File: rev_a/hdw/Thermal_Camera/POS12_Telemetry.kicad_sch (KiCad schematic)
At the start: 7 parts, among them U501 INA219BxDCN, U502 MCP9804

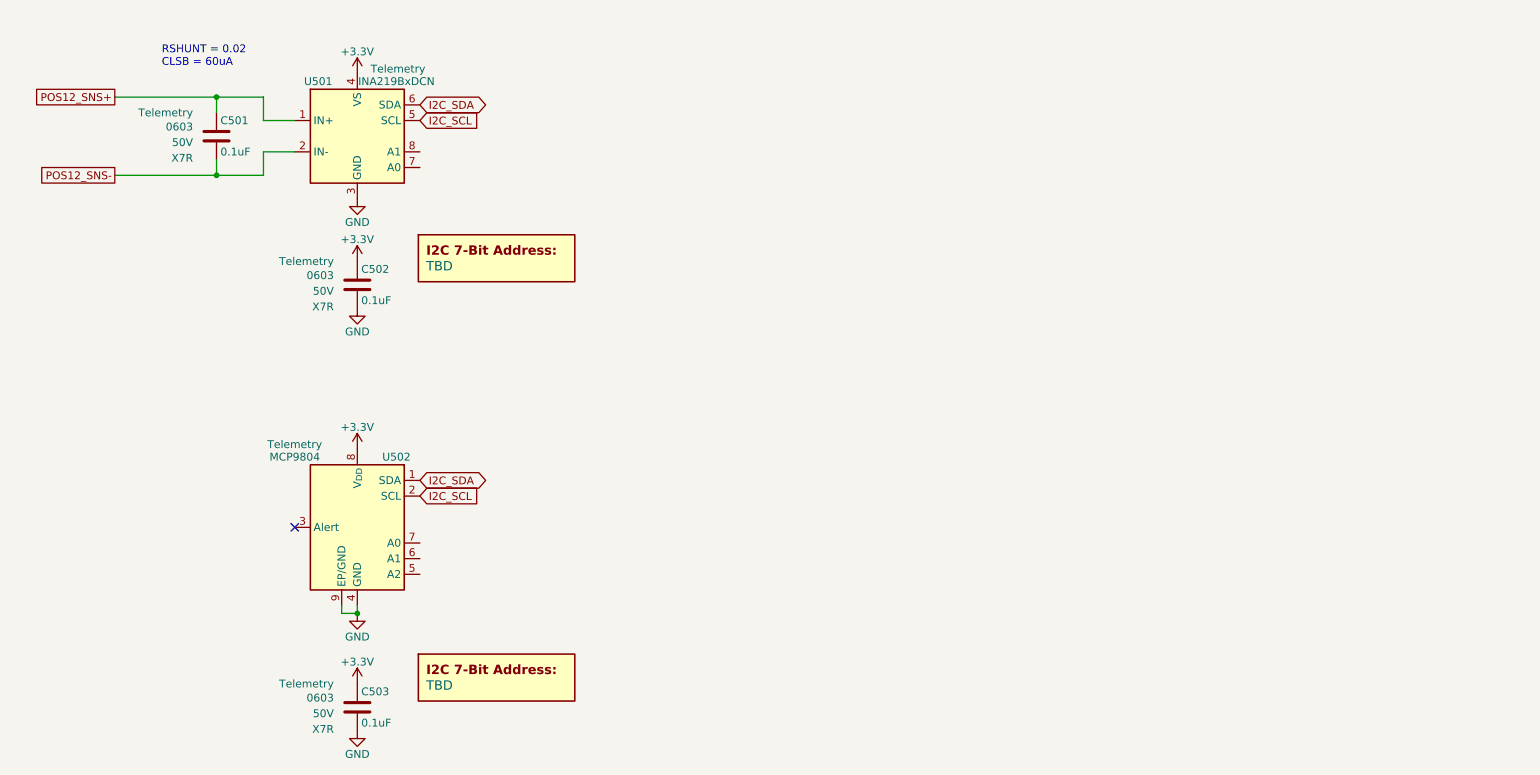
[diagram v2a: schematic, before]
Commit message: changed a lot of circuits from +3.3V to +3.0V VDD
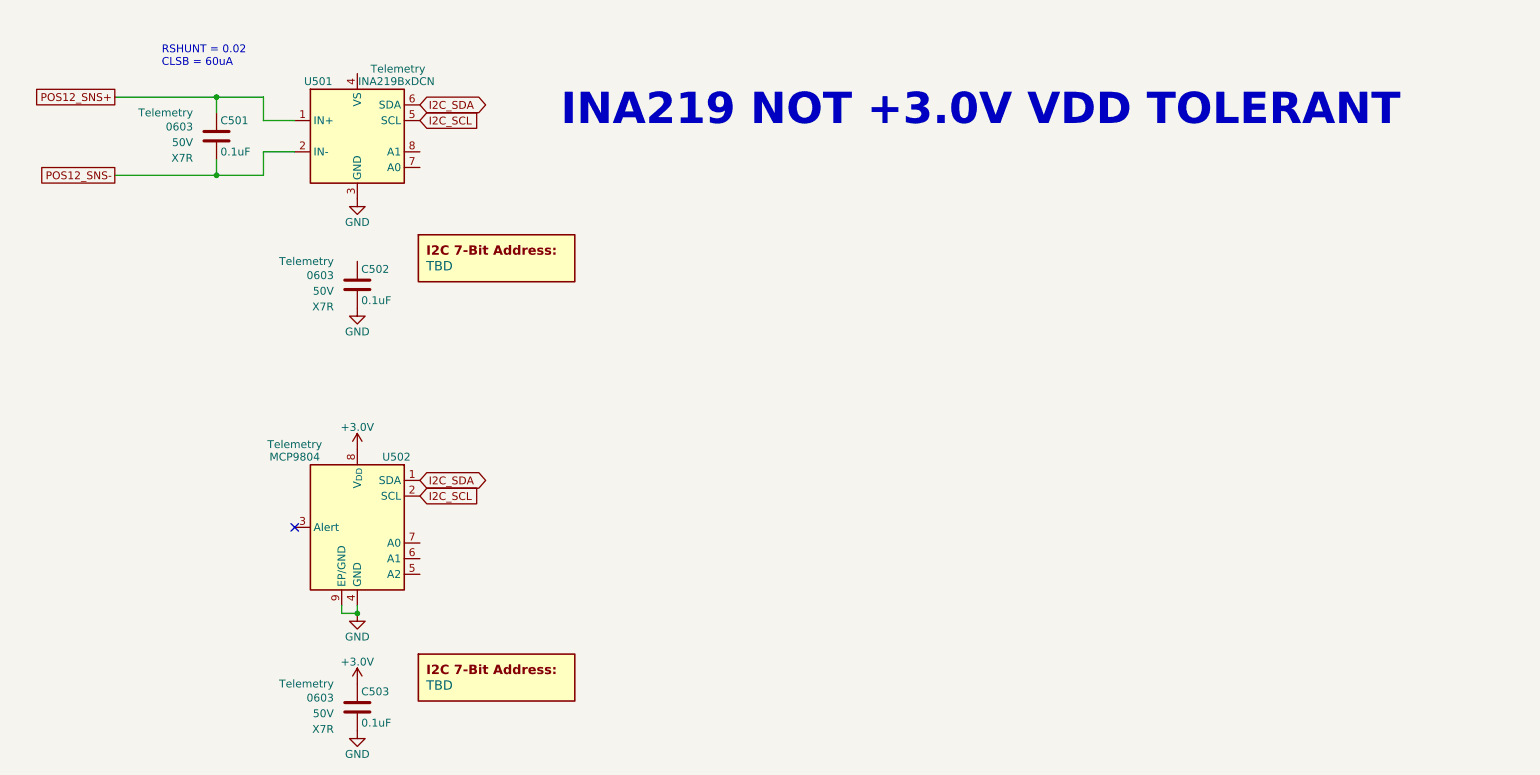
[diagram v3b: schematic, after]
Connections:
- net +3.3V renamed +3.0V
- net +3.0V: no longer C502.1, U501.4 (VS)
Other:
- note added: "INA219 NOT +3.0V VDD TOLERANT"
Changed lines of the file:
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@@
     (effects (font (size 1.27 1.27)) (justify left bottom))
+  )
+  (text "INA219 NOT +3.0V VDD TOLERANT" (at 168.91 50.8 0)
+    (effects (font (face "Courier New") (size 5.08 5.08) (thickness 0.508) bold (color 194 0 0 1)) (justify left bottom))
   )
   (global_label "I2C_SCL" (shape input) (at 146.05 49.53 0) (fields_autoplaced)
@@
     )
   )
+  (symbol (lib_id "Custom Library:+3.0V") (at 135.89 102.87 0) (unit 1)
+    (in_bom yes) (on_board yes) (dnp no)
+    (property "Reference" "#PWR0307" (at 135.89 106.68 0)
+      (effects (font (size 1.27 1.27)) hide)
+    )
+    (property "Value" "+3.0V" (at 135.89 99.314 0)
+      (effects (font (size 1.27 1.27)))
+    )
+    (property "Footprint" "" (at 135.89 102.87 0)
+      (effects (font (size 1.27 1.27)) hide)
+    )
+    (property "Datasheet" "" (at 135.89 102.87 0)
+      (effects (font (size 1.27 1.27)) hide)
+    )
+    (pin "1")
+    (instances
+      (project "Thermal_Camera"
+        (path "/4bd21e0b-5408-4b93-866e-c82ac5b31fa9/78c72208-6db1-4ab8-a8df-528bec958adb"
+          (reference "#PWR0307") (unit 1)
+        )
+      )
+    )
+  )
+  (symbol (lib_id "Custom Library:+3.0V") (at 135.89 140.97 0) (unit 1)
+    (in_bom yes) (on_board yes) (dnp no)
+    (property "Reference" "#PWR0305" (at 135.89 144.78 0)
+      (effects (font (size 1.27 1.27)) hide)
+    )
+    (property "Value" "+3.0V" (at 135.89 137.414 0)
+      (effects (font (size 1.27 1.27)))
+    )
+    (property "Footprint" "" (at 135.89 140.97 0)
+      (effects (font (size 1.27 1.27)) hide)
+    )
+    (property "Datasheet" "" (at 135.89 140.97 0)
+      (effects (font (size 1.27 1.27)) hide)
+    )
+    (pin "1")
+    (instances
+      (project "Thermal_Camera"
+        (path "/4bd21e0b-5408-4b93-866e-c82ac5b31fa9/78c72208-6db1-4ab8-a8df-528bec958adb"
+          (reference "#PWR0305") (unit 1)
+        )
+      )
+    )
+  )
   (symbol (lib_id "Custom_Library:C_Custom") (at 113.03 52.07 0) (unit 1)
     (in_bom yes) (on_board yes) (dnp no)
@@
         (path "/4bd21e0b-5408-4b93-866e-c82ac5b31fa9/78c72208-6db1-4ab8-a8df-528bec958adb"
           (reference "#PWR0302") (unit 1)
-        )
-      )
-    )
-  )
-  (symbol (lib_id "power:+3.3V") (at 135.89 102.87 0) (mirror y) (unit 1)
-    (in_bom yes) (on_board yes) (dnp no)
-    (property "Reference" "#PWR0505" (at 135.89 106.68 0)
-      (effects (font (size 1.27 1.27)) hide)
-    )
-    (property "Value" "+3.3V" (at 135.89 99.314 0)
-      (effects (font (size 1.27 1.27)))
-    )
-    (property "Footprint" "" (at 135.89 102.87 0)
-      (effects (font (size 1.27 1.27)) hide)
-    )
-    (property "Datasheet" "" (at 135.89 102.87 0)
-      (effects (font (size 1.27 1.27)) hide)
-    )
-    (pin "1")
-    (instances
-      (project "Nixie_Clock_Core"
-        (path "/16fdce21-b570-4d81-a458-e8839d611806/9c9d19c1-3649-44f4-8893-4087e4bbe058"
-          (reference "#PWR0505") (unit 1)
-        )
-      )
-      (project "LED_Panel_Controller"
-        (path "/22e05ee1-b227-4be7-9418-94433f274720/00000000-0000-0000-0000-00005e0a0e29"
-          (reference "#PWR?") (unit 1)
-        )
-        (path "/22e05ee1-b227-4be7-9418-94433f274720/00000000-0000-0000-0000-00005eae2d84"
-          (reference "#PWR?") (unit 1)
-        )
-        (path "/22e05ee1-b227-4be7-9418-94433f274720/00000000-0000-0000-0000-00005f581b77"
-          (reference "#PWR?") (unit 1)
-        )
-        (path "/22e05ee1-b227-4be7-9418-94433f274720/00000000-0000-0000-0000-00005e052856"
-          (reference "#PWR?") (unit 1)
-        )
-        (path "/22e05ee1-b227-4be7-9418-94433f274720/00000000-0000-0000-0000-00005e0652ba"
-          (reference "#PWR?") (unit 1)
-        )
-        (path "/22e05ee1-b227-4be7-9418-94433f274720/00000000-0000-0000-0000-00005f581b58"
-          (reference "#PWR?") (unit 1)
-        )
-      )
-      (project "Thermal_Camera"
-        (path "/4bd21e0b-5408-4b93-866e-c82ac5b31fa9/78c72208-6db1-4ab8-a8df-528bec958adb"
-          (reference "#PWR0305") (unit 1)
-        )
-      )
-    )
-  )
-  (symbol (lib_id "power:+3.3V") (at 135.89 72.39 0) (unit 1)
-    (in_bom yes) (on_board yes) (dnp no)
-    (property "Reference" "#PWR0503" (at 135.89 76.2 0)
-      (effects (font (size 1.27 1.27)) hide)
-    )
-    (property "Value" "+3.3V" (at 135.89 68.834 0)
-      (effects (font (size 1.27 1.27)))
-    )
-    (property "Footprint" "" (at 135.89 72.39 0)
-      (effects (font (size 1.27 1.27)) hide)
-    )
-    (property "Datasheet" "" (at 135.89 72.39 0)
-      (effects (font (size 1.27 1.27)) hide)
-    )
-    (pin "1")
-    (instances
-      (project "Nixie_Clock_Core"
-        (path "/16fdce21-b570-4d81-a458-e8839d611806/9c9d19c1-3649-44f4-8893-4087e4bbe058"
-          (reference "#PWR0503") (unit 1)
-        )
-      )
-      (project "LED_Panel_Controller"
-        (path "/22e05ee1-b227-4be7-9418-94433f274720/00000000-0000-0000-0000-00005e0a0e29"
-          (reference "#PWR?") (unit 1)
-        )
-        (path "/22e05ee1-b227-4be7-9418-94433f274720/00000000-0000-0000-0000-00005eae2d84"
-          (reference "#PWR?") (unit 1)
-        )
-        (path "/22e05ee1-b227-4be7-9418-94433f274720/00000000-0000-0000-0000-00005f581b77"
-          (reference "#PWR?") (unit 1)
-        )
-        (path "/22e05ee1-b227-4be7-9418-94433f274720/00000000-0000-0000-0000-00005e052856"
-          (reference "#PWR?") (unit 1)
-        )
-        (path "/22e05ee1-b227-4be7-9418-94433f274720/00000000-0000-0000-0000-00005e0652ba"
-          (reference "#PWR?") (unit 1)
-        )
-        (path "/22e05ee1-b227-4be7-9418-94433f274720/00000000-0000-0000-0000-00005f581b58"
-          (reference "#PWR?") (unit 1)
-        )
-      )
-      (project "Thermal_Camera"
-        (path "/4bd21e0b-5408-4b93-866e-c82ac5b31fa9/78c72208-6db1-4ab8-a8df-528bec958adb"
-          (reference "#PWR0303") (unit 1)
         )
       )
@@
     )
   )
-  (symbol (lib_id "power:+3.3V") (at 135.89 140.97 0) (unit 1)
-    (in_bom yes) (on_board yes) (dnp no)
-    (property "Reference" "#PWR0507" (at 135.89 144.78 0)
-      (effects (font (size 1.27 1.27)) hide)
-    )
-    (property "Value" "+3.3V" (at 135.89 137.414 0)
-      (effects (font (size 1.27 1.27)))
-    )
-    (property "Footprint" "" (at 135.89 140.97 0)
-      (effects (font (size 1.27 1.27)) hide)
-    )
-    (property "Datasheet" "" (at 135.89 140.97 0)
-      (effects (font (size 1.27 1.27)) hide)
-    )
-    (pin "1")
-    (instances
-      (project "Nixie_Clock_Core"
-        (path "/16fdce21-b570-4d81-a458-e8839d611806/9c9d19c1-3649-44f4-8893-4087e4bbe058"
-          (reference "#PWR0507") (unit 1)
-        )
-      )
-      (project "LED_Panel_Controller"
-        (path "/22e05ee1-b227-4be7-9418-94433f274720/00000000-0000-0000-0000-00005e0a0e29"
-          (reference "#PWR?") (unit 1)
-        )
-        (path "/22e05ee1-b227-4be7-9418-94433f274720/00000000-0000-0000-0000-00005eae2d84"
-          (reference "#PWR?") (unit 1)
-        )
-        (path "/22e05ee1-b227-4be7-9418-94433f274720/00000000-0000-0000-0000-00005f581b77"
-          (reference "#PWR?") (unit 1)
-        )
-        (path "/22e05ee1-b227-4be7-9418-94433f274720/00000000-0000-0000-0000-00005e052856"
-          (reference "#PWR?") (unit 1)
-        )
-        (path "/22e05ee1-b227-4be7-9418-94433f274720/00000000-0000-0000-0000-00005e0652ba"
-          (reference "#PWR?") (unit 1)
-        )
-        (path "/22e05ee1-b227-4be7-9418-94433f274720/00000000-0000-0000-0000-00005f581b58"
-          (reference "#PWR?") (unit 1)
-        )
-      )
-      (project "Thermal_Camera"
-        (path "/4bd21e0b-5408-4b93-866e-c82ac5b31fa9/78c72208-6db1-4ab8-a8df-528bec958adb"
-          (reference "#PWR0307") (unit 1)
-        )
-      )
-    )
-  )
   (symbol (lib_id "Custom_Library:I2C_Address") (at 158.496 73.152 0) (unit 1)
     (in_bom yes) (on_board yes) (dnp no)
@@
         )
       )
-    )
-  )
-  (symbol (lib_id "power:+3.3V") (at 135.89 41.91 0) (unit 1)
-    (in_bom yes) (on_board yes) (dnp no)
-    (property "Reference" "#PWR0501" (at 135.89 45.72 0)
-      (effects (font (size 1.27 1.27)) hide)
-    )
-    (property "Value" "+3.3V" (at 135.89 38.354 0)
-      (effects (font (size 1.27 1.27)))
-    )
-    (property "Footprint" "" (at 135.89 41.91 0)
-      (effects (font (size 1.27 1.27)) hide)
-    )
-    (property "Datasheet" "" (at 135.89 41.91 0)
-      (effects (font (size 1.27 1.27)) hide)
-    )
-    (pin "1")
-    (instances
-      (project "Nixie_Clock_Core"
-        (path "/16fdce21-b570-4d81-a458-e8839d611806/9c9d19c1-3649-44f4-8893-4087e4bbe058"
-          (reference "#PWR0501") (unit 1)
-        )
-      )
-      (project "LED_Panel_Controller"
-        (path "/22e05ee1-b227-4be7-9418-94433f274720/00000000-0000-0000-0000-00005e0a0e29"
-          (reference "#PWR?") (unit 1)
-        )
-        (path "/22e05ee1-b227-4be7-9418-94433f274720/00000000-0000-0000-0000-00005eae2d84"
-          (reference "#PWR?") (unit 1)
-        )
-        (path "/22e05ee1-b227-4be7-9418-94433f274720/00000000-0000-0000-0000-00005f581b77"
-          (reference "#PWR?") (unit 1)
-        )
-        (path "/22e05ee1-b227-4be7-9418-94433f274720/00000000-0000-0000-0000-00005e052856"
-          (reference "#PWR?") (unit 1)
-        )
-        (path "/22e05ee1-b227-4be7-9418-94433f274720/00000000-0000-0000-0000-00005e0652ba"
-          (reference "#PWR?") (unit 1)
-        )
-        (path "/22e05ee1-b227-4be7-9418-94433f274720/00000000-0000-0000-0000-00005f581b58"
-          (reference "#PWR?") (unit 1)
-        )
-      )
-      (project "Thermal_Camera"
-        (path "/4bd21e0b-5408-4b93-866e-c82ac5b31fa9/78c72208-6db1-4ab8-a8df-528bec958adb"
-          (reference "#PWR0301") (unit 1)
-        )
-      )
